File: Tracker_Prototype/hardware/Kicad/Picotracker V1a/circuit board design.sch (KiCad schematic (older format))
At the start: 35 parts, among them J1 Conn_01x06, J2 GND, J3 3.3V, SW1 SW_Push, U1 MAX-M8C, U3 CMWX1ZZABZ-078, U6 MS5607-02BA

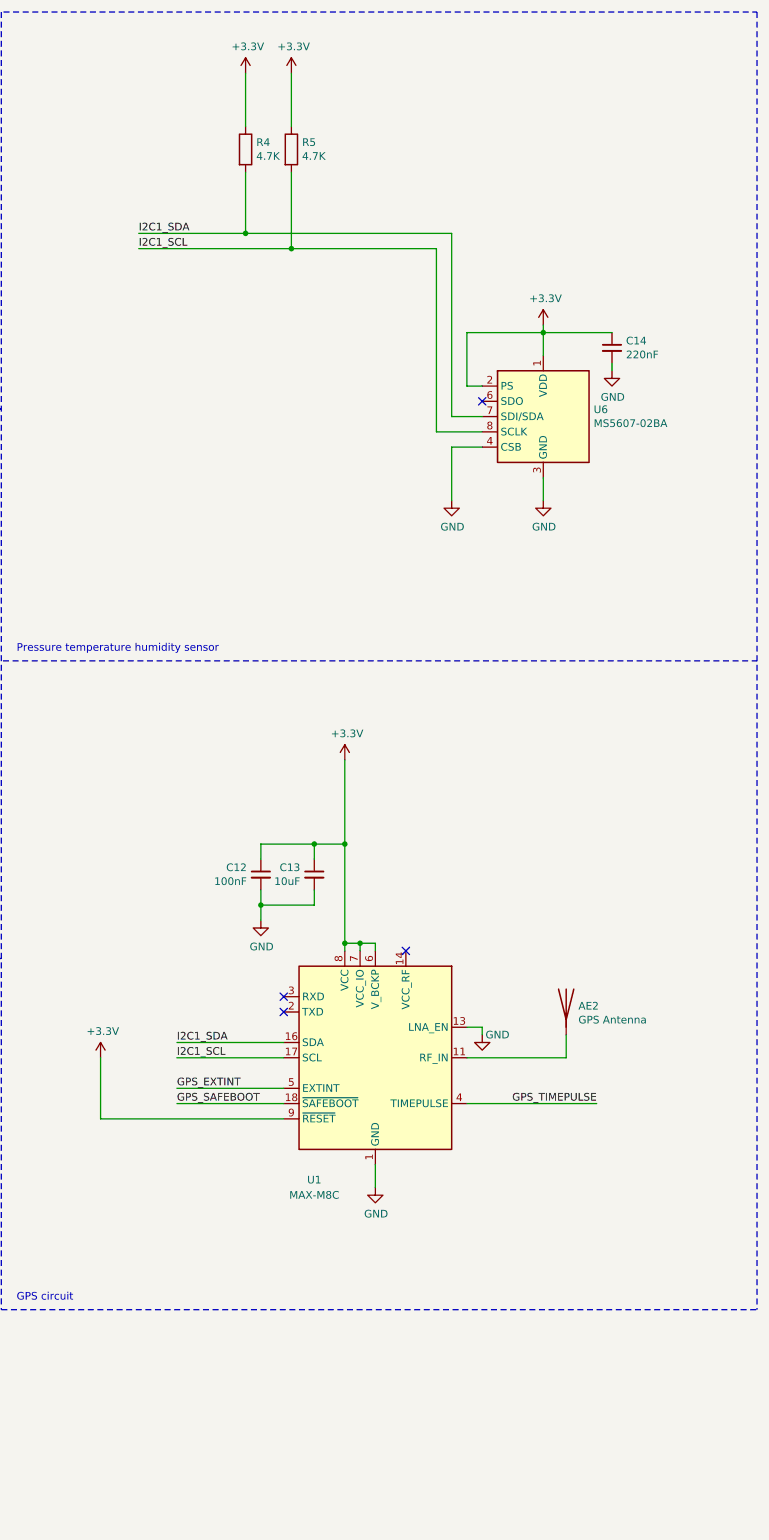
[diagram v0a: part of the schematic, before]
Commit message: Routed most of the b variant of the board
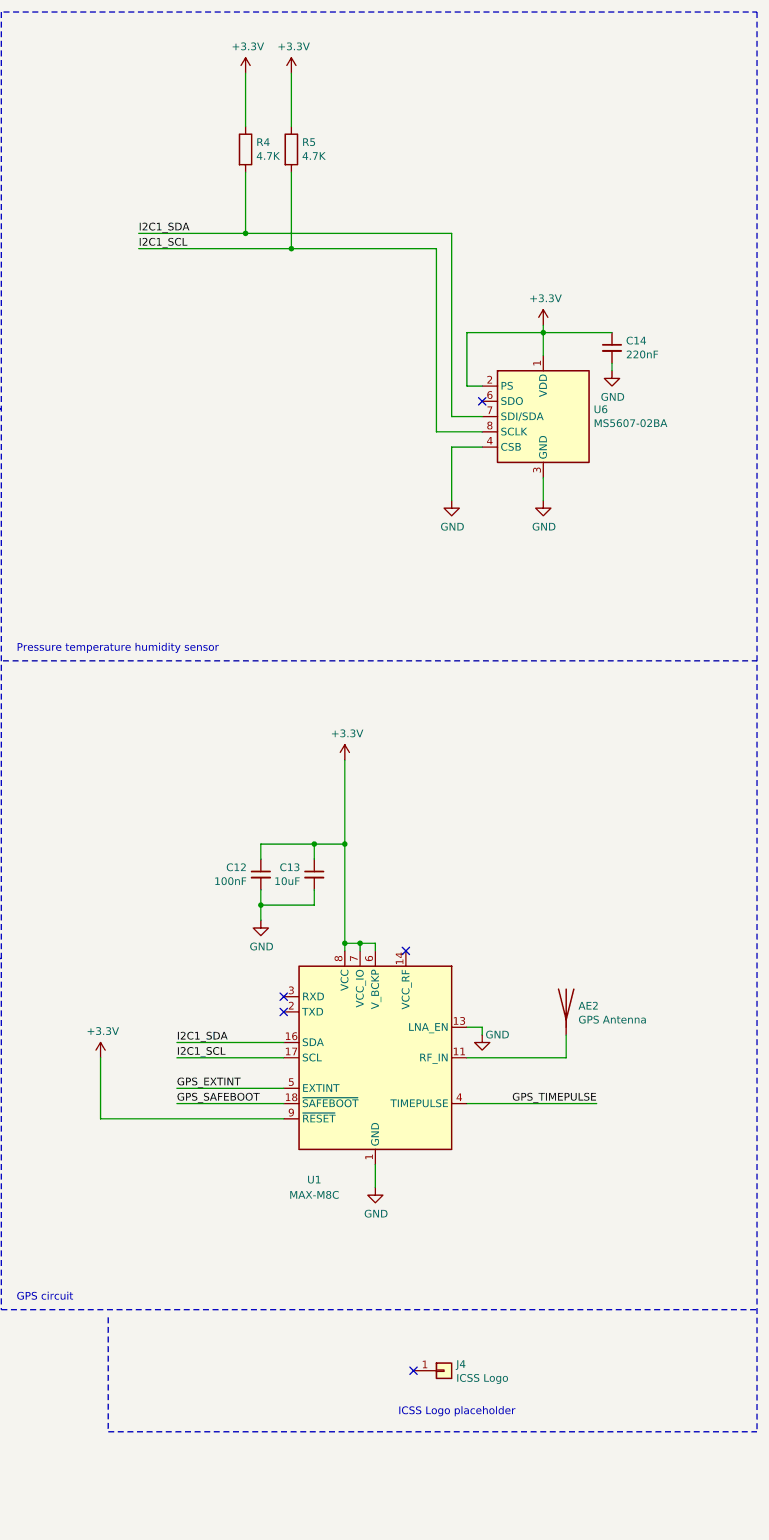
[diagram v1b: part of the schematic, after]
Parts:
- added J4: ICSS Logo, flight-computer:ICSS_Logo, symbol Connector_Generic:Conn_01x01
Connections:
- no-connect marks 32 -> 33
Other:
- note added: "ICSS Logo placeholder\n"
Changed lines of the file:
@@
 Wire Notes Line
 	11100 650  11100 9150
-Wire Notes Line
-	16050 650  16050 9150
 Text Notes 3050 6550 0    50   ~ 0
 Main Microcontroller + Lora tranceiver\n
@@
 Wire Wire Line
 	7150 3100 7800 3100
+$Comp
+L Connector_Generic:Conn_01x01 J4
+U 1 1 5DBBDDA8
+P 14000 9550
+F 0 "J4" H 14080 9592 50  0000 L CNN
+F 1 "ICSS Logo" H 14080 9501 50  0000 L CNN
+F 2 "flight-computer:ICSS_Logo" H 14000 9550 50  0001 C CNN
+F 3 "~" H 14000 9550 50  0001 C CNN
+	1    14000 9550
+	1    0    0    -1
+$EndComp
+Text Notes 13700 9850 0    50   ~ 0
+ICSS Logo placeholder\n
+Wire Notes Line
+	11800 9200 11800 9950
+Wire Notes Line
+	11800 9950 16050 9950
+Wire Notes Line
+	16050 650  16050 9950
+NoConn ~ 13800 9550
 $EndSCHEMATC

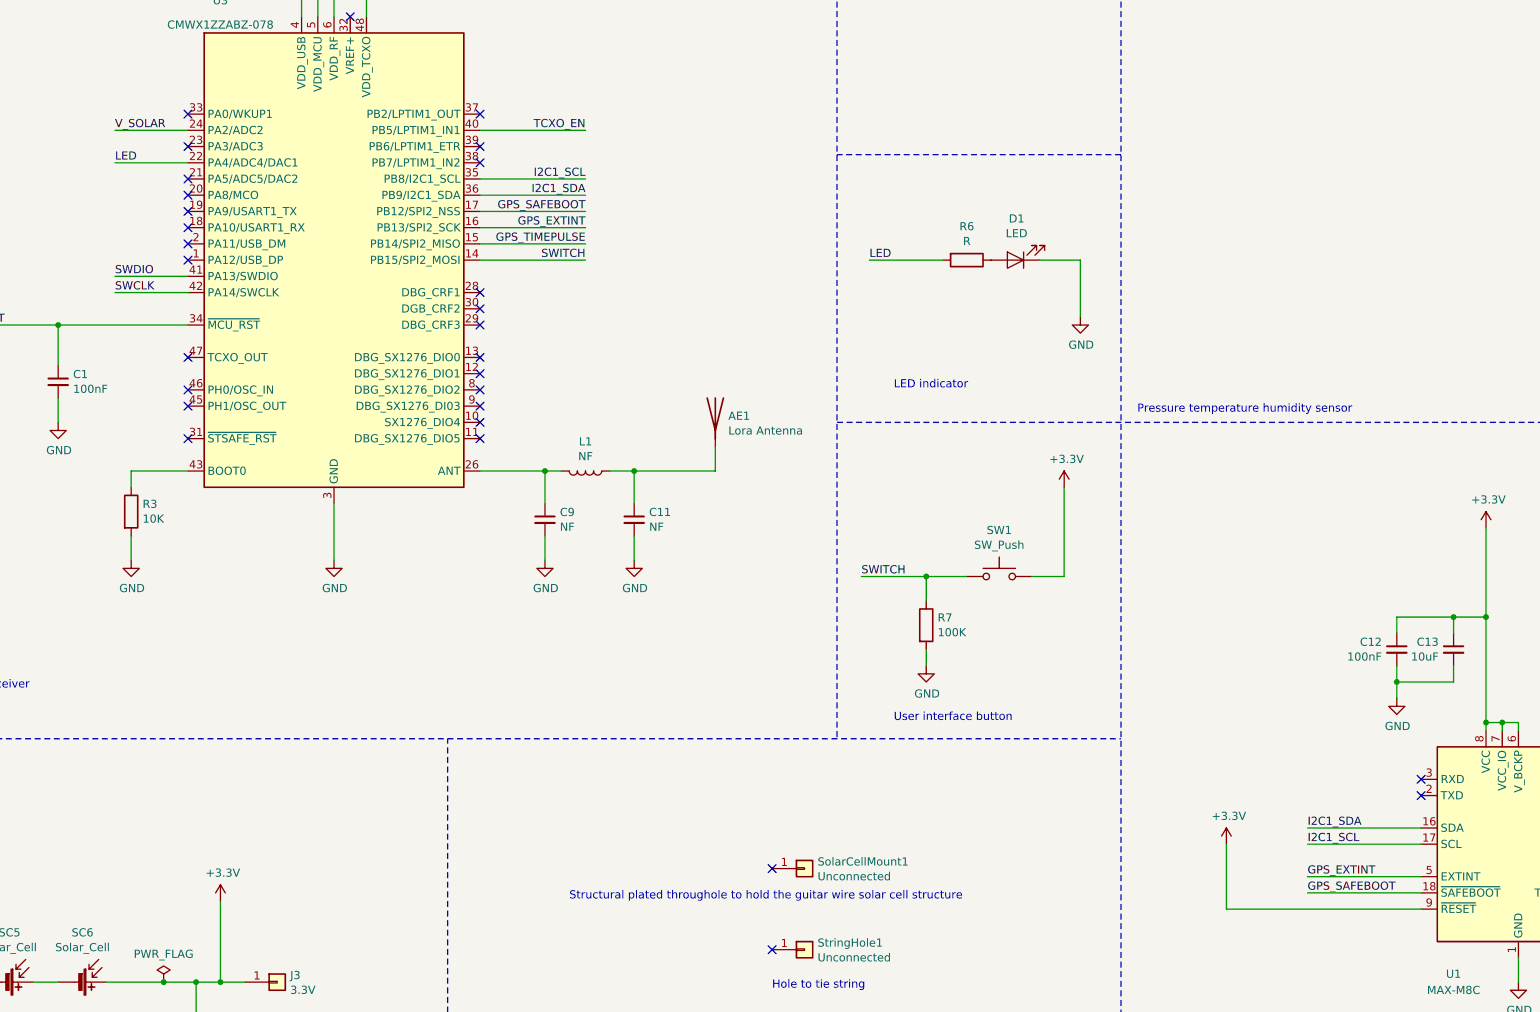
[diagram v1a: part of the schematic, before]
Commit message: rerouted the "a" variant to place the RF output pin of abz module closer to antenna
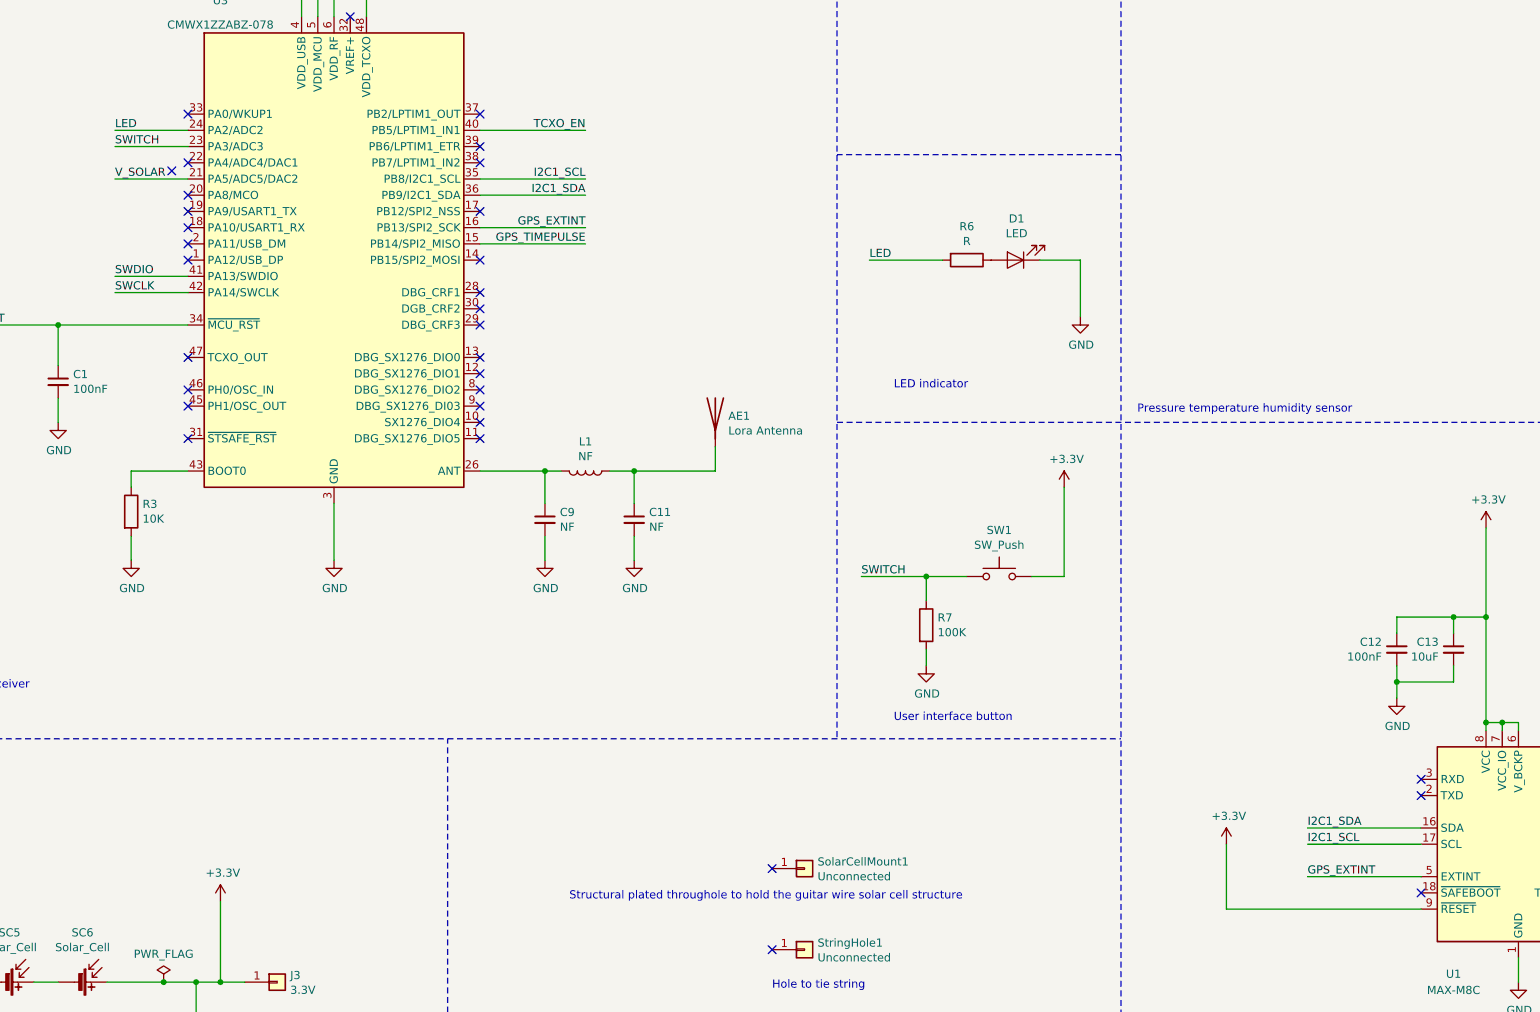
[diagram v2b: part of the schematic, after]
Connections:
- net LED: now also U3.24 (PA2/ADC2); no longer U3.22 (PA4/ADC4/DAC1)
- net SWITCH: now also U3.23 (PA3/ADC3); no longer U3.14 (PB15/SPI2_MOSI)
- net V_SOLAR: now also U3.21 (PA5/ADC5/DAC2); no longer U3.24 (PA2/ADC2)
- net GPS_SAFEBOOT: no longer names the net of U3.17 (PB12/SPI2_NSS)
- net GPS_SAFEBOOT: no longer U1.18 (~SAFEBOOT)
- no-connect marks 33 -> 36
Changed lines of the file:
@@
 Wire Wire Line
 	7150 3400 7800 3400
-Wire Wire Line
-	7150 3500 7800 3500
 $Comp
 L power:GND #PWR?
@@
 Text Label 7800 3400 2    50   ~ 0
 I2C1_SCL
-Text Label 7800 3500 2    50   ~ 0
-I2C1_SDA
 Wire Wire Line
 	8600 5200 8600 5050
@@
 	13450 6750 13550 6750
 Connection ~ 13450 6750
-Wire Wire Line
-	7150 3600 7800 3600
 Wire Wire Line
 	7150 3700 7800 3700
@@
 	1    0    0    -1
 $EndComp
-Text Label 12250 7800 0    50   ~ 0
-GPS_SAFEBOOT
-Text Label 7800 3600 2    50   ~ 0
-GPS_SAFEBOOT
 Text Label 12250 7700 0    50   ~ 0
 GPS_EXTINT
@@
 NoConn ~ 5350 3600
 NoConn ~ 5350 3500
-NoConn ~ 5350 3400
-NoConn ~ 5350 3200
 NoConn ~ 5350 3000
-Wire Wire Line
-	12950 7900 11750 7900
 Wire Wire Line
 	13350 6750 13350 6800
@@
 NoConn ~ 12950 7100
 NoConn ~ 12950 7200
-Wire Wire Line
-	12950 7800 12250 7800
 Wire Wire Line
 	12250 7500 12950 7500
@@
 Structural plated throughole to hold the guitar wire solar cell structure
 Wire Wire Line
-	5350 3100 4900 3100
-Text Label 4900 3100 0    50   ~ 0
-V_SOLAR
-Wire Wire Line
 	4750 1350 6050 1350
 NoConn ~ 5350 3700
@@
 NoConn ~ 5350 3900
 Wire Wire Line
-	5350 3300 4900 3300
+	5350 3100 4900 3100
 Wire Wire Line
 	10850 3900 10850 4250
@@
 $EndComp
 Wire Wire Line
-	7150 3900 7800 3900
-Text Label 7800 3900 2    50   ~ 0
+	5350 3200 4900 3200
+Text Label 4900 3200 0    50   ~ 0
 SWITCH
 Wire Notes Line
@@
 Wire Notes Line
 	9350 650  9350 6850
-Text Label 4900 3300 0    50   ~ 0
+Text Label 4900 3100 0    50   ~ 0
 LED
 Text Label 9550 3900 0    50   ~ 0
@@
 	16050 650  16050 9950
 NoConn ~ 13800 9550
+Text Label 4900 3400 0    50   ~ 0
+V_SOLAR
+Wire Wire Line
+	5350 3400 4900 3400
+NoConn ~ 7150 3900
+NoConn ~ 5250 3350
+NoConn ~ 5350 3300
+Wire Wire Line
+	12950 7900 11750 7900
+NoConn ~ 12950 7800
+Text Label 7800 3500 2    50   ~ 0
+I2C1_SDA
+Wire Wire Line
+	7150 3500 7800 3500
+NoConn ~ 7150 3600
 $EndSCHEMATC
